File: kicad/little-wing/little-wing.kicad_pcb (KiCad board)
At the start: 4 copper layers, 16.1 x 57.1 mm, 65 parts, among them J1 HRO_TYPE-C-31-M-14, J2 Battery, J3 rgb, J4 columns, J5 Conn_01x10, J6 rows, J7 sensor, Q1 AO3401A, Q2 2N7002, SW1 Battery, SW2 Reset, U1 nRF52840_CKAA, U2 nPM1100-CAAx, X1 32MHz, X2 32.768kHz

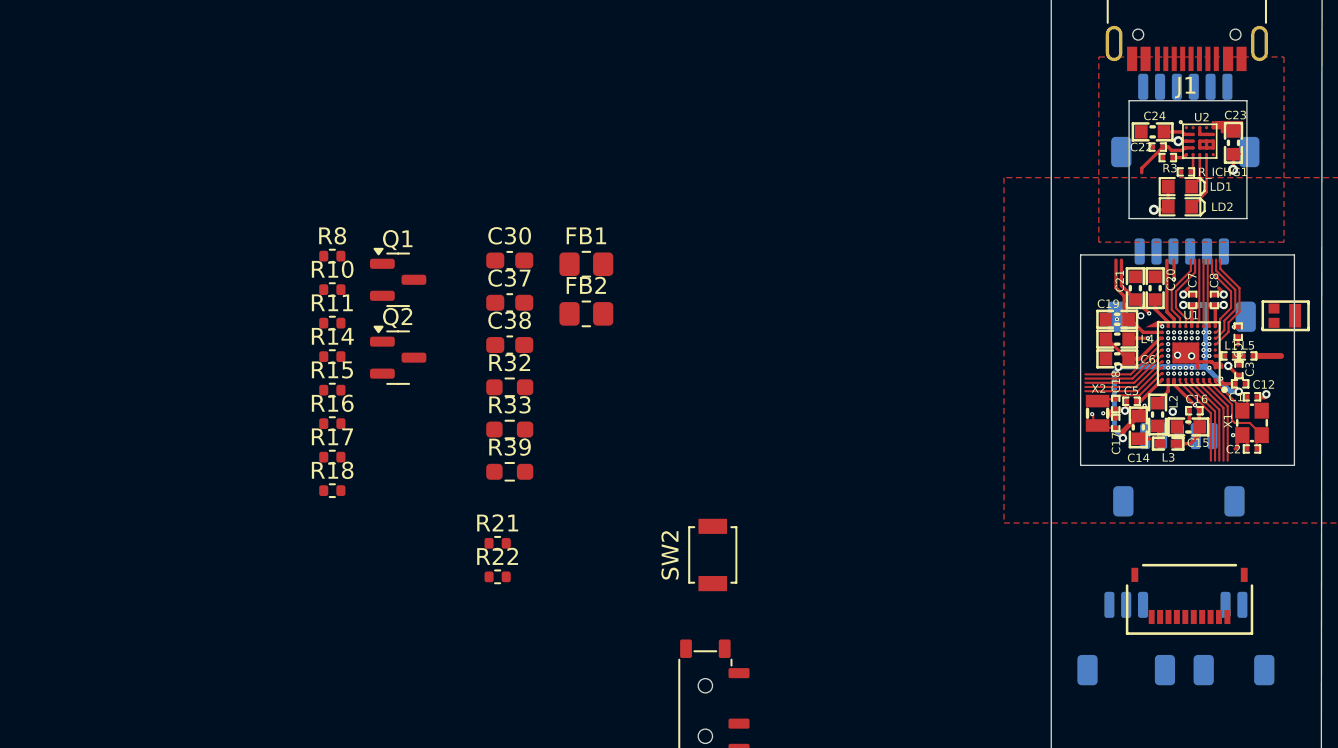
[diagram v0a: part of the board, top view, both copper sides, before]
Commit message: Reseting all the extra components sizes
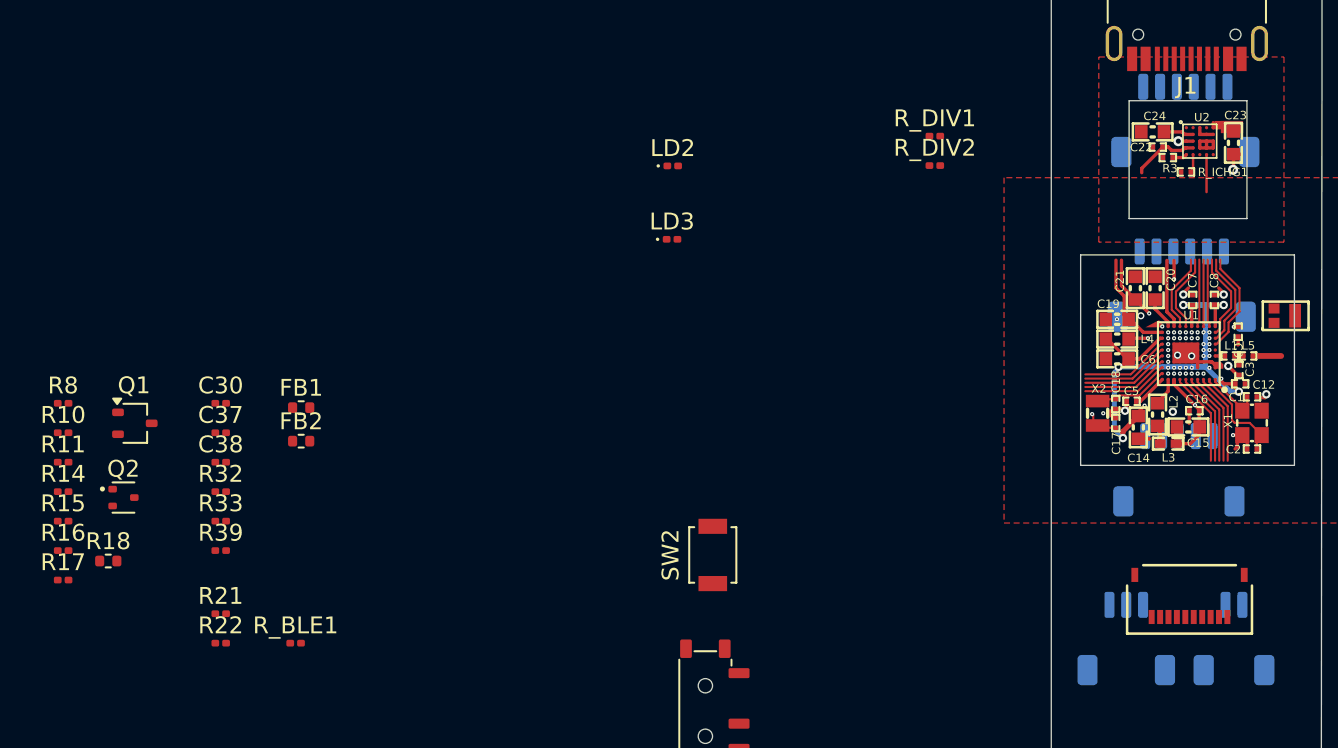
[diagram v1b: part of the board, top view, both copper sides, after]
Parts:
- removed LD1: L0603R, pcblib:LED_0603_R
- added LD3: L0603 (Blue), LED_SMD:LED_0201_0603Metric, F.Cu at (119.4, 74.9)
- added R_BLE1: 470k, Resistor_SMD:R_0201_0603Metric, F.Cu at (97.1, 98.9)
- added R_DIV1: 2M, Resistor_SMD:R_0201_0603Metric, F.Cu at (135.0, 68.8)
- added R_DIV2: 806k, Resistor_SMD:R_0201_0603Metric, F.Cu at (135.0, 70.5)
- C30, C37, C38: footprint Capacitor_SMD:C_0603_1608Metric_Pad1.08x0.95mm_HandSolder -> Capacitor_SMD:C_0201_0603Metric
- FB1, FB2: footprint Resistor_SMD:R_0805_2012Metric_Pad1.20x1.40mm_HandSolder -> Resistor_SMD:R_0402_1005Metric
- LD2: value L0603G -> L0603G (Amber); footprint pcblib:LED_0603_G -> LED_SMD:LED_0201_0603Metric
- Q1: footprint Package_TO_SOT_SMD:SOT-23 -> Package_TO_SOT_SMD:SOT-323_SC-70
- Q2: footprint Package_TO_SOT_SMD:SOT-23 -> Package_TO_SOT_SMD:SOT-523
- R10, R11, R14, R15, R16, R17, R21, R22, R8: footprint Resistor_SMD:R_0402_1005Metric -> Resistor_SMD:R_0201_0603Metric
- R32, R33, R39: footprint Resistor_SMD:R_0603_1608Metric_Pad0.98x0.95mm_HandSolder -> Resistor_SMD:R_0201_0603Metric
- moved LD2 30.2 mm to (119.5, 70.6), turned to 0 degrees
- moved C30 19.1 mm to (92.6, 84.7)
- moved FB1 19.0 mm to (97.4, 84.9)
- moved C37 18.8 mm to (92.6, 86.4)
- moved FB2 18.6 mm to (97.4, 86.9)
- moved C38 18.5 mm to (92.6, 88.2)
- moved Q2 18.3 mm to (86.8, 90.3)
- moved R32 18.3 mm to (92.6, 89.9)
- moved R8 18.2 mm to (83.3, 84.7)
- moved R10 18.1 mm to (83.3, 86.4)
- moved R33 18.0 mm to (92.6, 91.7)
- moved R11 18.0 mm to (83.3, 88.2)
- moved R14 17.9 mm to (83.3, 89.9)
- moved Q1 17.8 mm to (87.5, 85.8)
- moved R39 17.8 mm to (92.6, 93.4)
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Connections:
- C21 pad 1: VBUS -> VSYS
- C24 pad 2: VBUS -> VSYS
- J1 pad A4: VBUS -> VSYS
- J1 pad A9: VBUS -> VSYS
- J1 pad B4: VBUS -> VSYS
- J1 pad B9: VBUS -> VSYS
- U1 pad C8: VSENS -> VSENSE
- U1 pad J9: VBUS -> VSYS
- U2 pad B1: VBUS -> VSYS
- U2 pad B2: VBUS -> VSYS
- U2 pad E3: /Main Module/PSU/ERR -> unconnected-(U2-ERR-PadE3)
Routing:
- net VBUS: track 7.55 -> 0.00 mm, vias 2 -> 0
- net VSENSE: track 0.00 -> 7.05 mm, vias 0 -> 2
- net VSENS: track 7.05 -> 0.00 mm, vias 2 -> 0
- net /Main Module/PSU/ERR: track 2.11 -> 0.00 mm
- net /Main Module/PSU/CHG: track 3.48 -> 2.22 mm
- net VSYS: track 19.3 -> 20.0 mm, vias 3 -> 4

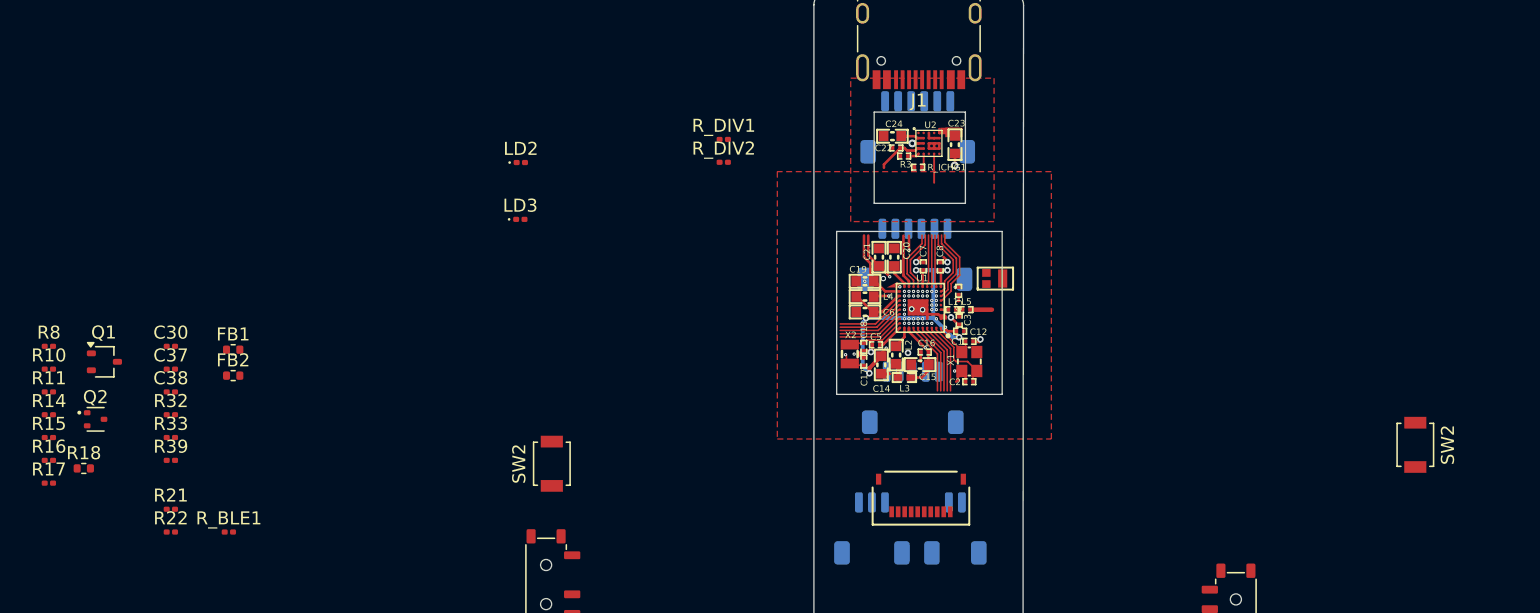
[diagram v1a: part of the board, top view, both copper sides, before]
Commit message: Dissolving and re-packaging the PSU block
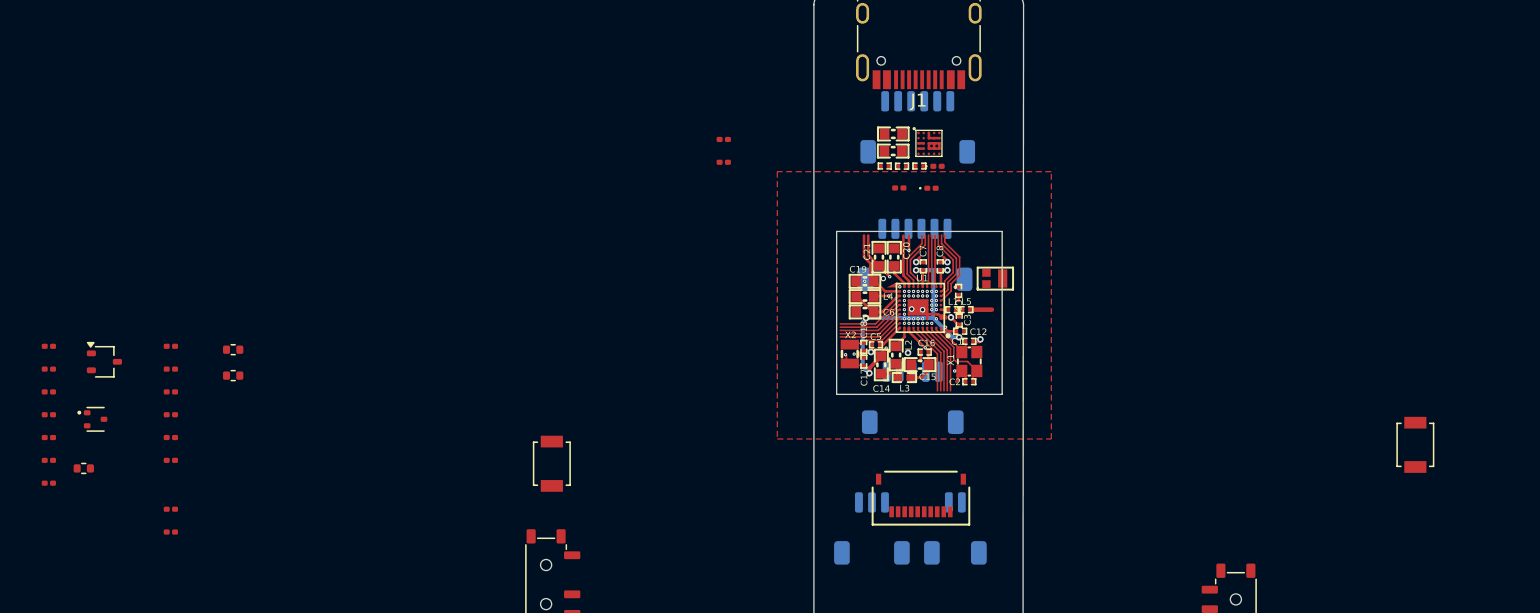
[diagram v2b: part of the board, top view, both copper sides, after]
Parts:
- moved R_BLE1 57.8 mm to (148.5, 72.5)
- moved LD2 32.0 mm to (151.4, 70.8)
- moved LD3 31.6 mm to (151.0, 72.5)
- moved C23 4.77 mm to (148.0, 69.7), turned to 0 degrees
- moved C22 1.65 mm to (147.4, 70.8)
- moved R3 0.79 mm to (148.7, 70.8)
- moved C24 0.18 mm to (148.1, 68.4)
- moved R_ICHG1 0.13 mm to (150.1, 70.8), turned to 180 degrees
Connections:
- C24 pad 2: VSYS -> VBUS
- U2 pad B1: VSYS -> VBUS
- U2 pad B2: VSYS -> VBUS
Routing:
- net VSYS: track 20.0 -> 12.3 mm, vias 4 -> 2
- net VBAT: track 3.98 -> 0.40 mm
- net /Main Module/PSU/CHG: track 2.22 -> 0.00 mm
- net GND: track 19.3 -> 17.9 mm
- net Net-(U2-ICHG): track 1.08 -> 0.00 mm
- net Net-(U2-NTC): track 0.89 -> 0.00 mm
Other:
- outline, holes or cut-outs redrawn

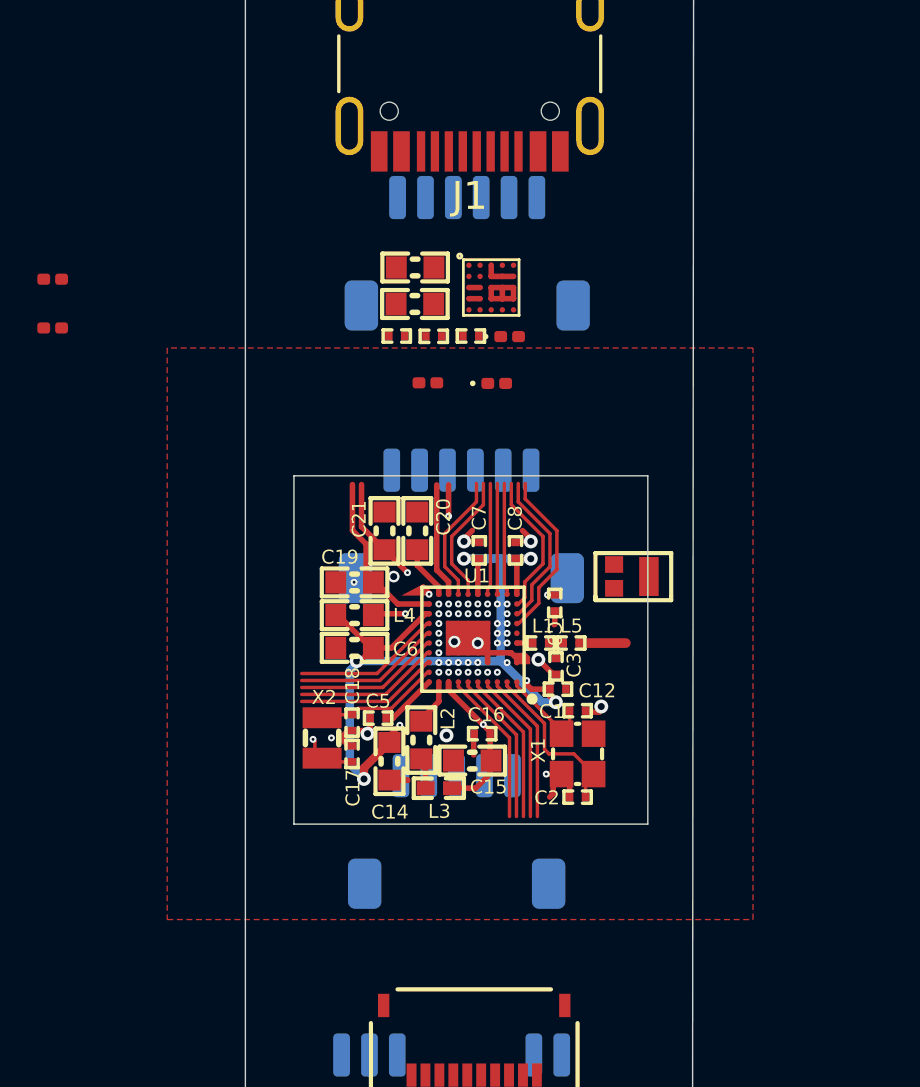
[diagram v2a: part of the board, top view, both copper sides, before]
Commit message: Unshielding the main block
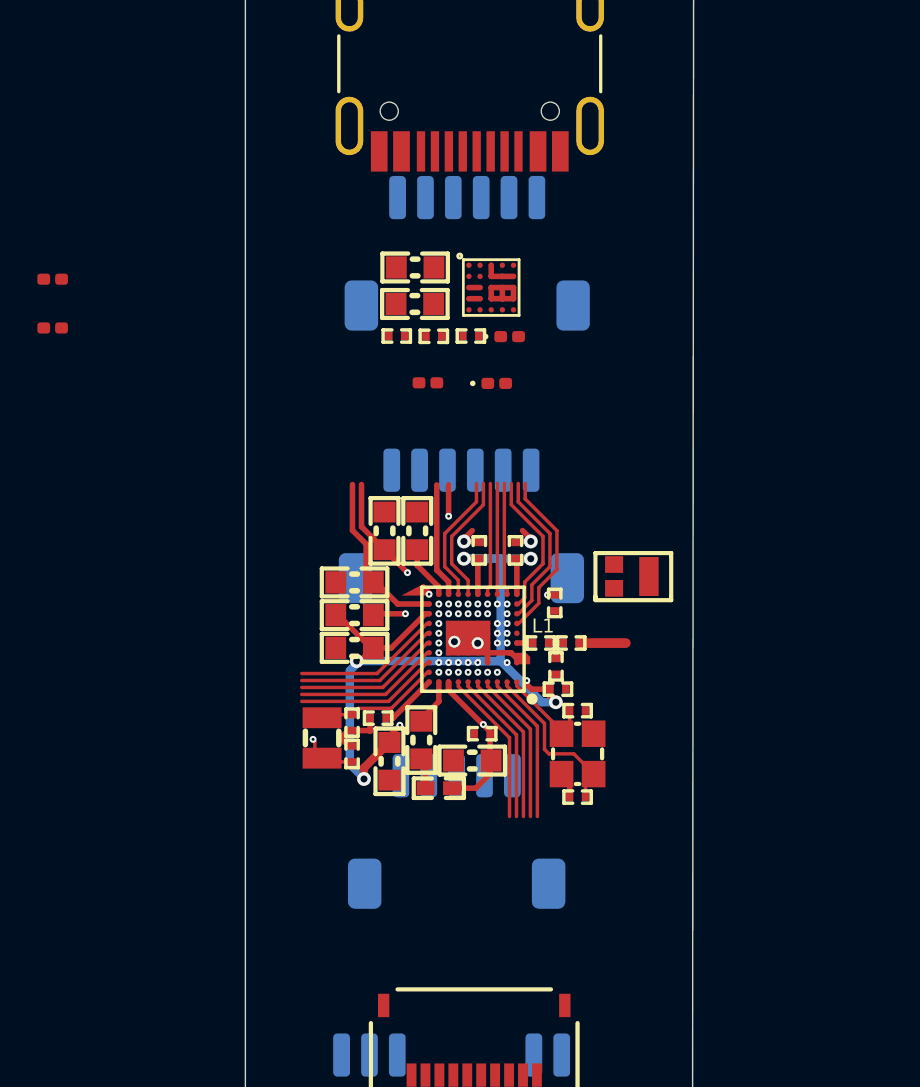
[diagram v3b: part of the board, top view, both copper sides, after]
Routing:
- net GND: track 17.9 -> 13.6 mm, vias 14 -> 6
- removed copper zone on F.Cu, net GND
- removed copper zone on In1.Cu, net GND
- removed copper zone on In2.Cu, net GND
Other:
- outline, holes or cut-outs redrawn

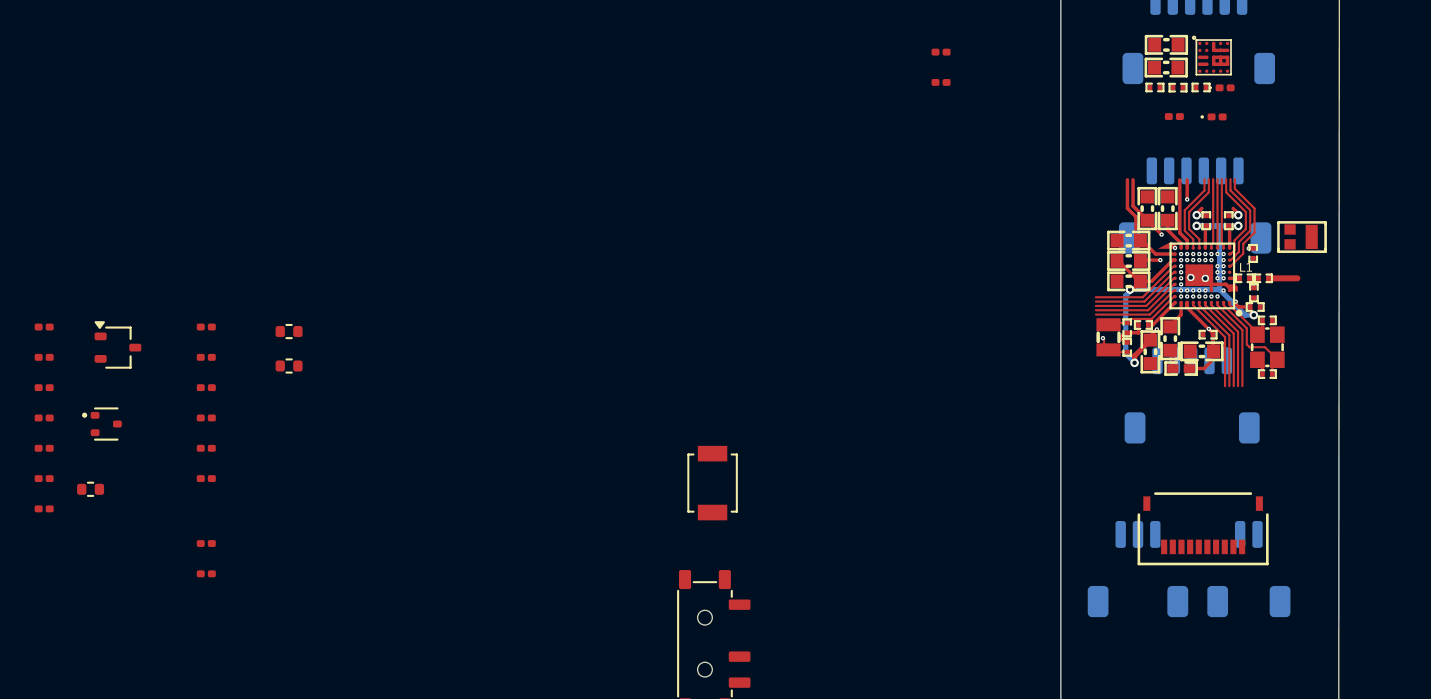
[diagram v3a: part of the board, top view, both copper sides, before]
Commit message: Swapping the crystals for smaller ones
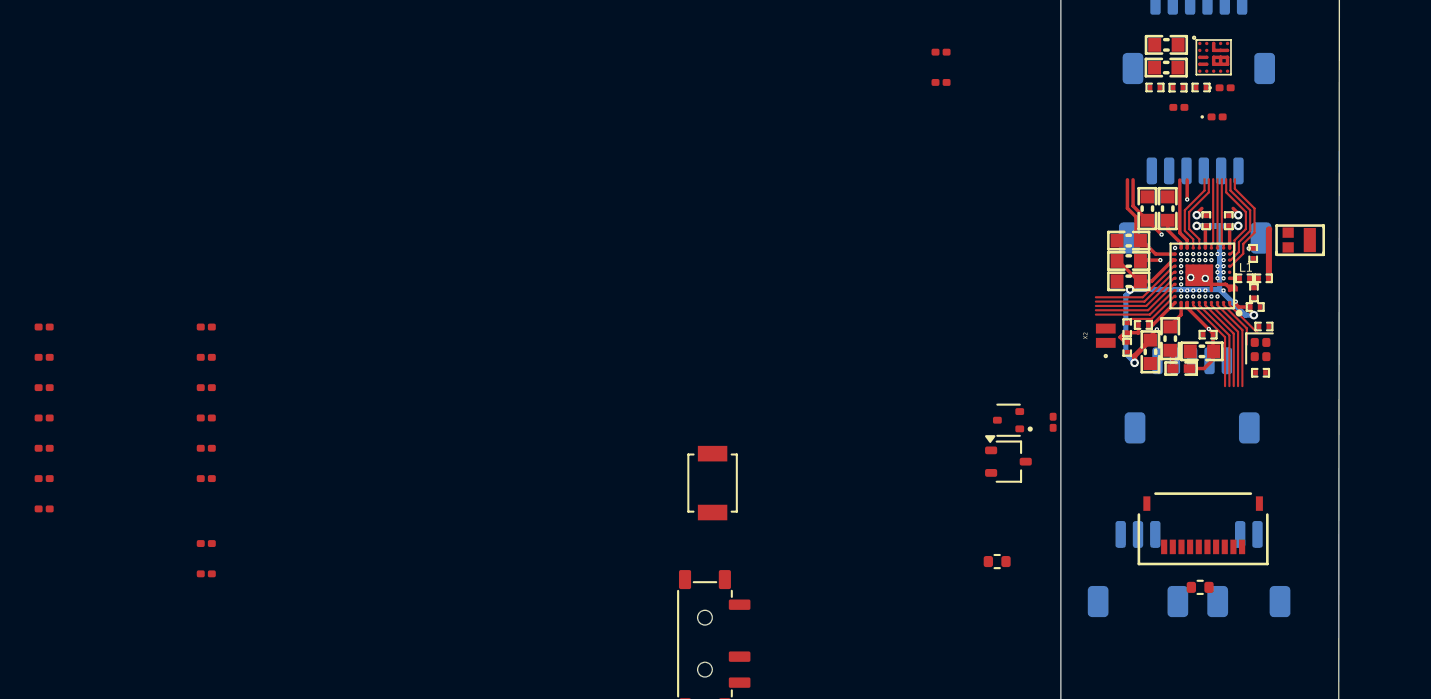
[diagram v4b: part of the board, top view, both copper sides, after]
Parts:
- R18: footprint Resistor_SMD:R_0402_1005Metric -> Resistor_SMD:R_0201_0603Metric
- X1: footprint Crystal_Osc$:BT-XTAL_2016 -> Crystal:Crystal_SMD_1210-4Pin_1.2x1.0mm
- X2: footprint Crystal_Osc$:XTAL_2012 -> EXC-1210:XTAL_ECS32761210TR
- moved R18 55.7 mm to (141.5, 90.2), turned to 90 degrees
- moved FB1 54.6 mm to (150.0, 99.7), turned to 180 degrees
- moved Q2 52.1 mm to (138.9, 90.0), turned to 180 degrees
- moved Q1 51.8 mm to (138.9, 92.4)
- moved FB2 42.4 mm to (138.3, 98.2)
- moved R_BLE1 0.59 mm to (148.8, 72.0)
- moved X1 0.42 mm to (153.5, 86.0), turned to 0 degrees
- moved C1 0.41 mm to (153.7, 84.6)
- moved C2 0.40 mm to (153.5, 87.3)
- moved AE1 0.21 mm to (155.7, 79.7)
- moved X2 0.19 mm to (144.6, 85.2)
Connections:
- C24 pad 2: VBUS -> VSYS
- U2 pad B1: VBUS -> VSYS
- U2 pad B2: VBUS -> VSYS
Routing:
- net Net-(U1-P0.00/XL1): track 7.42 -> 4.37 mm, vias 2 -> 1
- net Net-(U1-XC2): track 5.77 -> 2.97 mm
- net Net-(U1-P0.01/XL2): track 4.83 -> 3.40 mm
- net GND: track 13.6 -> 12.2 mm
- net /Main Module/MCU/RF: track 1.64 -> 2.84 mm
- net Net-(U1-XC1): track 3.41 -> 2.41 mm

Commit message: Dialing in the physical package
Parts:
- SW2 (x2): footprint Button_Switch_SMD:SW_SPST_B3U-1000P -> Button_Switch_SMD:SW_SPST_B3U-3000P
- moved R10 83.3 mm to (166.6, 86.5)
- moved R17 82.5 mm to (165.5, 88.2)
- moved FB2 56.9 mm to (170.6, 51.4), turned to 180 degrees
- moved FB1 53.2 mm to (161.3, 47.7), turned to 0 degrees
- moved C30 48.9 mm to (138.9, 69.0)
- moved C37 48.9 mm to (138.9, 70.8)
- moved C38 48.9 mm to (138.9, 72.5)
- moved R21 48.9 mm to (138.9, 81.5)
- moved R22 48.9 mm to (138.9, 83.2)
- moved R32 48.9 mm to (138.9, 74.2)
- moved R33 48.9 mm to (138.9, 76.0)
- moved R39 48.9 mm to (138.9, 77.8)
- moved R11 48.9 mm to (129.6, 72.5)
- moved R14 48.9 mm to (129.6, 74.2)
- moved R15 48.9 mm to (129.6, 76.0)
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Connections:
- J7 pad 1: VDD -> GND
- J7 pad 6: GND -> VDD
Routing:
- net VDD: track 37.2 -> 17.1 mm
- net unconnected-(U1-P0.03/AIN1-PadA5): track 5.50 -> 0.00 mm
- net unconnected-(U1-P1.13-PadA4): track 5.46 -> 0.00 mm
- net unconnected-(U1-P1.11-PadA3): track 5.42 -> 0.00 mm
- net Net-(U1-XC2): track 2.97 -> 0.15 mm
- net Net-(U1-XC1): track 2.41 -> 0.14 mm
- net /Main Module/MCU/RF: track 2.84 -> 4.40 mm
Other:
- board size 16.1 x 57.1 mm -> 14 x 42.1 mm
- board text added: "Screen"
- board text added: "body offset"
